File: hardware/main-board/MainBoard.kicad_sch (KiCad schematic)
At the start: 14 parts, among them J1 Conn_01x03_Pin, J2 Conn_01x03_Pin, J3 Conn_01x03_Pin, J4 Conn_01x03_Pin, SW1 SW_SP3T, SW2 SW_SP3T, U1 MT8816AF1, U2 TL081, U3 TL071, U4 TL071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

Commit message: Updated Footprints and Controls
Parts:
- U2, U3, U4, U5, U6: footprint (none) -> Package_SO:SOIC-8_3.9x4.9mm_P1.27mm
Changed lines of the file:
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@@
 			)
 		)
-		(property "Footprint" ""
+		(property "Footprint" "Package_SO:SOIC-8_3.9x4.9mm_P1.27mm"
 			(at 252.73 40.64 0)
 			(effects
@@
 			)
 		)
-		(property "Footprint" ""
+		(property "Footprint" "Package_SO:SOIC-8_3.9x4.9mm_P1.27mm"
 			(at 252.73 67.31 0)
 			(effects
@@
 			)
 		)
-		(property "Footprint" ""
+		(property "Footprint" "Package_SO:SOIC-8_3.9x4.9mm_P1.27mm"
 			(at 252.73 120.65 0)
 			(effects
@@
 			)
 		)
-		(property "Footprint" ""
+		(property "Footprint" "Package_SO:SOIC-8_3.9x4.9mm_P1.27mm"
 			(at 252.73 93.98 0)
 			(effects
@@
 			)
 		)
-		(property "Footprint" ""
+		(property "Footprint" "Package_SO:SOIC-8_3.9x4.9mm_P1.27mm"
 			(at 190.5 40.64 0)
 			(effects

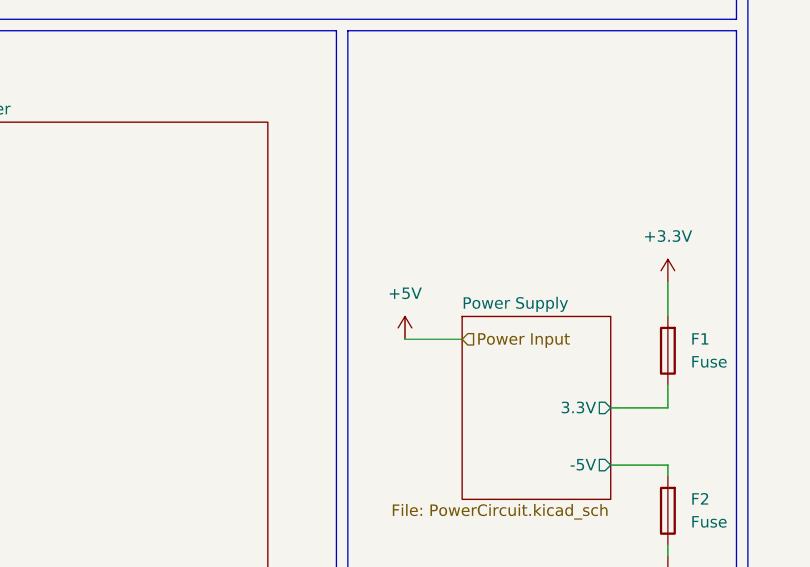
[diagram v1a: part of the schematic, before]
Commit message: Designated majority of footprints
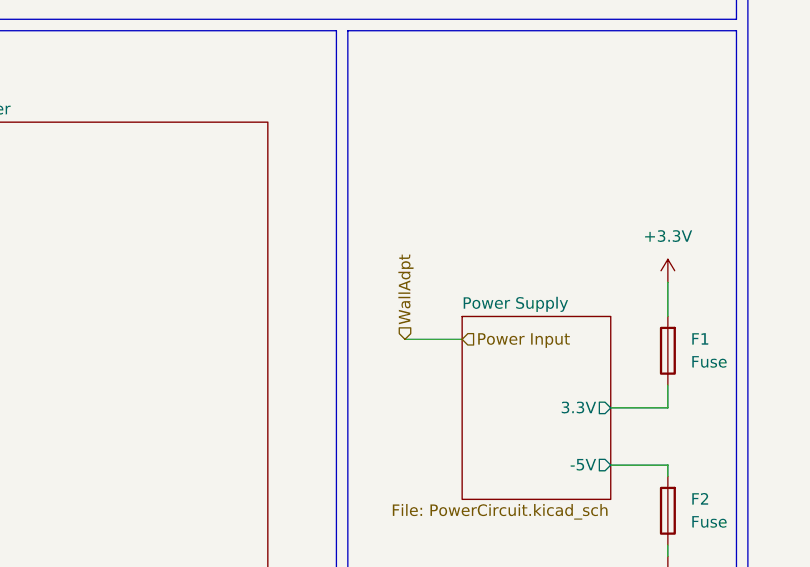
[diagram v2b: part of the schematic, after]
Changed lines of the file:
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@@
+		)
+	)
+	(hierarchical_label "WallAdpt"
+		(shape input)
+		(at 182.88 113.03 90)
+		(effects
+			(font
+				(size 1.27 1.27)
+			)
+			(justify left)
 		)
 	)
@@
 					(unit 1)
 				)
-			)
-		)
-	)
-	(symbol
-		(lib_id "power:+5V")
-		(at 182.88 113.03 0)
-		(unit 1)
-		(exclude_from_sim no)
-		(in_bom yes)
-		(on_board yes)
-		(dnp no)
-		(fields_autoplaced yes)
-		(property "Reference" "#PWR03"
-			(at 182.88 116.84 0)
-			(effects
-				(font
-					(size 1.27 1.27)
-				)
-				(hide yes)
-			)
-		)
-		(property "Value" "+5V"
-			(at 182.88 107.95 0)
-			(effects
-				(font
-					(size 1.27 1.27)
-				)
-			)
-		)
-		(property "Footprint" ""
-			(at 182.88 113.03 0)
-			(effects
-				(font
-					(size 1.27 1.27)
-				)
-				(hide yes)
-			)
-		)
-		(property "Datasheet" ""
-			(at 182.88 113.03 0)
-			(effects
-				(font
-					(size 1.27 1.27)
-				)
-				(hide yes)
-			)
-		)
-		(property "Description" "Power symbol creates a global label with name \"+5V\""
-			(at 182.88 113.03 0)
-			(effects
-				(font
-					(size 1.27 1.27)
-				)
-				(hide yes)
-			)
-		)
-		(pin "1"
-		)
-		(instances
-			(project ""
-				(path "/5dd933ff-bc57-4741-8957-85d8c6e75130"
-					(reference "#PWR03")
-					(unit 1)
-				)

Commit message: Fully filled footprints
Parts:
- F1, F2: footprint (none) -> Fuse:Fuse_0603_1608Metric_Pad1.05x0.95mm_HandSolder
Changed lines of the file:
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@@
 			)
 		)
-		(property "Footprint" ""
+		(property "Footprint" "Fuse:Fuse_0603_1608Metric_Pad1.05x0.95mm_HandSolder"
 			(at 213.868 132.08 90)
 			(effects
@@
 			)
 		)
-		(property "Footprint" ""
+		(property "Footprint" "Fuse:Fuse_0603_1608Metric_Pad1.05x0.95mm_HandSolder"
 			(at 213.868 114.3 90)
 			(effects

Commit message: PCB comps in, and formatted
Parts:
- J1, J2, J3, J4: footprint Connector_PinHeader_1.00mm:PinHeader_1x32_P1.00mm_Horizontal -> Connector_PinHeader_1.00mm:PinHeader_1x03_P1.00mm_Horizontal
- U1: footprint MT8816AF1:QFP80P1200X1200X120-44N -> SeniorDesignFP:QFP80P1200X1200X120-44N
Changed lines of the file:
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@@
 			)
 		)
-		(property "Footprint" "Connector_PinHeader_1.00mm:PinHeader_1x32_P1.00mm_Horizontal"
+		(property "Footprint" "Connector_PinHeader_1.00mm:PinHeader_1x03_P1.00mm_Horizontal"
 			(at 49.53 111.76 0)
 			(effects
@@
 			)
 		)
-		(property "Footprint" "Connector_PinHeader_1.00mm:PinHeader_1x32_P1.00mm_Horizontal"
+		(property "Footprint" "Connector_PinHeader_1.00mm:PinHeader_1x03_P1.00mm_Horizontal"
 			(at 49.53 97.79 0)
 			(effects
@@
 			)
 		)
-		(property "Footprint" "Connector_PinHeader_1.00mm:PinHeader_1x32_P1.00mm_Horizontal"
+		(property "Footprint" "Connector_PinHeader_1.00mm:PinHeader_1x03_P1.00mm_Horizontal"
 			(at 81.28 166.37 0)
 			(effects
@@
 			)
 		)
-		(property "Footprint" "MT8816AF1:QFP80P1200X1200X120-44N"
+		(property "Footprint" "SeniorDesignFP:QFP80P1200X1200X120-44N"
 			(at 82.804 88.392 0)
 			(effects
@@
 			)
 		)
-		(property "Footprint" "Connector_PinHeader_1.00mm:PinHeader_1x32_P1.00mm_Horizontal"
+		(property "Footprint" "Connector_PinHeader_1.00mm:PinHeader_1x03_P1.00mm_Horizontal"
 			(at 81.28 156.21 0)
 			(effects

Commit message: designed Power PCB section layout
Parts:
- removed U1: MT8816AF1, SeniorDesignFP:QFP80P1200X1200X120-44N, symbol SeniorDesign:MT8816AF1
- added F1: 500mA, Fuse:Fuse_0603_1608Metric_Pad1.05x0.95mm_HandSolder, symbol Device:Fuse
- added U1: CD22M3494MQZ, SeniorDesignFP:PLCC44_16P66X16P66_INR-M, symbol SeniorDesign:CD22M3494MQZ
- F2: value Fuse -> 500mA
- F3: renamed from F1; value Fuse -> 500mA
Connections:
- net +5V: now also F1.2
- net Cell_0_Buff: now also U1.35 (Y1)
- net Cell_1_Buff: now also U1.37 (Y2)
- net Cell_2_Buff: now also U1.39 (Y3)
- net Cell_3_Buff: now also U1.17 (Y4)
- net STD/Input_1: now also U1.31 (X0)
- net STD/Input_2: now also U1.30 (X1)
- net STD/Input_3: now also U1.29 (X2)
- net STD1/Input_1: now also U1.28 (X3)
- net STD1/Input_2: now also U1.27 (X4)
- net STD1/Input_3: now also U1.26 (X5)
- net STD2/Input_1: now also U1.8 (X10)
- net STD2/Input_2: now also U1.9 (X11)
- net STD2/Input_3: now also U1.25 (X12)
- net STD3/Input_1: now also U1.5 (X7)
- net STD3/Input_2: now also U1.6 (X8)
- net STD3/Input_3: now also U1.7 (X9)
- net Signal_In: now also U1.32 (Y0)
- net at U2.3 (+): now also U1.4 (X6)
- new net Power Supply/5V: F1.1
- no-connect marks 0 -> 16
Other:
- sheet Power Supply ports: added 5V; removed none
- moved on the sheet: F3

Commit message: Added wiring to cells and compacted input
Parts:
- J1, J2, J3, J4: footprint Connector_PinHeader_1.00mm:PinHeader_1x03_P1.00mm_Horizontal -> Connector_PinHeader_2.54mm:PinHeader_1x03_P2.54mm_Vertical
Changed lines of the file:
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@@
 			)
 		)
-		(property "Footprint" "Connector_PinHeader_1.00mm:PinHeader_1x03_P1.00mm_Horizontal"
+		(property "Footprint" "Connector_PinHeader_2.54mm:PinHeader_1x03_P2.54mm_Vertical"
 			(at 49.53 111.76 0)
 			(effects
@@
 			)
 		)
-		(property "Footprint" "Connector_PinHeader_1.00mm:PinHeader_1x03_P1.00mm_Horizontal"
+		(property "Footprint" "Connector_PinHeader_2.54mm:PinHeader_1x03_P2.54mm_Vertical"
 			(at 49.53 97.79 0)
 			(effects
@@
 			)
 		)
-		(property "Footprint" "Connector_PinHeader_1.00mm:PinHeader_1x03_P1.00mm_Horizontal"
+		(property "Footprint" "Connector_PinHeader_2.54mm:PinHeader_1x03_P2.54mm_Vertical"
 			(at 81.28 166.37 0)
 			(effects
@@
 			)
 		)
-		(property "Footprint" "Connector_PinHeader_1.00mm:PinHeader_1x03_P1.00mm_Horizontal"
+		(property "Footprint" "Connector_PinHeader_2.54mm:PinHeader_1x03_P2.54mm_Vertical"
 			(at 81.28 156.21 0)
 			(effects

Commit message: Standard cell 1 finalizations
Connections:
- net STD/Input_1 renamed STD_Y2
- net STD/Input_2 renamed STD_Y1
- net STD/Input_3 renamed STD_Y0
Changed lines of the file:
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@@
+	(wire
+		(pts
+			(xy 96.52 29.21) (xy 97.79 29.21)
+		)
+		(stroke
+			(width 0)
+			(type default)
+		)
+	)
 	(wire
 		(pts
@@
 	(wire
 		(pts
-			(xy 90.17 27.94) (xy 90.17 25.4)
-		)
-		(stroke
-			(width 0)
-			(type default)
-		)
-	)
-	(wire
-		(pts
 			(xy 55.88 156.21) (xy 76.2 156.21)
 		)
@@
 	(wire
 		(pts
-			(xy 88.9 21.59) (xy 97.79 21.59)
-		)
-		(stroke
-			(width 0)
-			(type default)
-		)
-	)
-	(wire
-		(pts
 			(xy 266.7 121.92) (xy 278.13 121.92)
 		)
@@
 	(wire
 		(pts
-			(xy 78.74 30.48) (xy 91.44 30.48)
-		)
-		(stroke
-			(width 0)
-			(type default)
-		)
-	)
-	(wire
-		(pts
 			(xy 142.24 57.15) (xy 148.59 57.15)
 		)
@@
 	(wire
 		(pts
-			(xy 90.17 25.4) (xy 97.79 25.4)
-		)
-		(stroke
-			(width 0)
-			(type default)
-		)
-	)
-	(wire
-		(pts
 			(xy 78.74 50.8) (xy 92.71 50.8)
 		)
@@
 	(wire
 		(pts
-			(xy 78.74 25.4) (xy 88.9 25.4)
-		)
-		(stroke
-			(width 0)
-			(type default)
-		)
-	)
-	(wire
-		(pts
 			(xy 266.7 41.91) (xy 278.13 41.91)
 		)
@@
 	(wire
 		(pts
-			(xy 91.44 29.21) (xy 91.44 30.48)
-		)
-		(stroke
-			(width 0)
-			(type default)
-		)
-	)
-	(wire
-		(pts
 			(xy 85.09 35.56) (xy 78.74 35.56)
 		)
@@
 	(wire
 		(pts
-			(xy 97.79 29.21) (xy 91.44 29.21)
-		)
-		(stroke
-			(width 0)
-			(type default)
-		)
-	)
-	(wire
-		(pts
 			(xy 238.76 29.21) (xy 266.7 29.21)
 		)
@@
 	(wire
 		(pts
+			(xy 96.52 25.4) (xy 97.79 25.4)
+		)
+		(stroke
+			(width 0)
+			(type default)
+		)
+	)
+	(wire
+		(pts
 			(xy 208.28 114.3) (xy 205.74 114.3)
 		)
@@
 	(wire
 		(pts
-			(xy 78.74 27.94) (xy 90.17 27.94)
+			(xy 96.52 21.59) (xy 97.79 21.59)
 		)
 		(stroke
@@
 	(wire
 		(pts
-			(xy 88.9 25.4) (xy 88.9 21.59)
-		)
-		(stroke
-			(width 0)
-			(type default)
-		)
-	)
-	(wire
-		(pts
 			(xy 81.28 39.37) (xy 181.61 39.37)
 		)
@@
 			(width 0)
 			(type default)
+		)
+	)
+	(label "STD_Y0"
+		(at 96.52 21.59 180)
+		(effects
+			(font
+				(size 1.27 1.27)
+			)
+			(justify right)
 		)
 	)
@@
 		)
 	)
+	(label "STD_Y0"
+		(at 78.74 30.48 0)
+		(effects
+			(font
+				(size 1.27 1.27)
+			)
+			(justify left)
+		)
+	)
 	(label "Cell_3_Buff"
 		(at 43.18 36.83 180)
@@
 		)
 	)
+	(label "STD_Y2"
+		(at 78.74 25.4 0)
+		(effects
+			(font
+				(size 1.27 1.27)
+			)
+			(justify left)
+		)
+	)
 	(label "Cell_0_Buff"
 		(at 43.18 29.21 180)
@@
 		)
 	)
+	(label "STD_Y1"
+		(at 78.74 27.94 0)
+		(effects
+			(font
+				(size 1.27 1.27)
+			)
+			(justify left)
+		)
+	)
 	(label "Signal_In"
 		(at 91.44 97.79 0)
@@
 		(effects
 			(font
+				(size 1.27 1.27)
+			)
+			(justify right)
+		)
+	)
+	(label "STD_Y1"
+		(at 96.52 25.4 180)
+		(effects
+			(font
+				(size 1.27 1.27)
+			)
+			(justify right)
+		)
+	)
+	(label "STD_Y2"
+		(at 96.52 29.21 180)
+		(effects
+			(font

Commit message: Standard cell 2
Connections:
- net STD2_Y0: now reaches U1.2 (X14)
- net STD2_Y1: now reaches U1.3 (X15)
- net STD2_Y2: now reaches U1.4 (X6)
- net STD2_Y2: no longer U2.3 (+)
- net STD1/Input_1 renamed STD1_Y2
- net STD1/Input_2 renamed STD1_Y1
- net STD1/Input_3 renamed STD1_Y0
- net STD2/Input_1 renamed STD_Out
- net STD_Out: now also U2.3 (+)
- net STD2/Input_2: no longer names the net of U1.9 (X11)
- net STD2/Input_3: no longer names the net of U1.25 (X12)
- no-connect marks 16 -> 14
